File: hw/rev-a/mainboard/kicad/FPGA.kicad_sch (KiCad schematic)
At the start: 46 parts, among them J17 PMOD1, J18 PMOD2, J19 PROG, J4 BUS_EXPANSION, J9 FPGA_MCU, Q1 MMBT3904, SW3 CONFIG, U10 T8Q144C3

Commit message: hw: ren rev-c -> rev-a
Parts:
- removed C61: 10u, Capacitor_SMD:C_0603_1608Metric, symbol Device:C_Small
- added C66: 4u7 10V, Capacitor_SMD:C_0402_1005Metric, symbol Device:C_Small
- C62, C63, C64, C65: value 10u -> 4u7 10V; footprint Capacitor_SMD:C_0603_1608Metric -> Capacitor_SMD:C_0402_1005Metric; LCSC C96446 -> C23733
- D7: LCSC C72043 -> C2986059
- J17, J18: footprint PET:PMOD_Socket_2x06_P2.54mm_Horizontal -> EconoPET:PMOD_Socket_2x06_P2.54mm_Horizontal
- R26: renamed from R19; value 12k 1% -> 12k
- RN10, RN9: value 10k -> 10kx4
- SW3: footprint Button_Switch_THT:SW_DIP_SPSTx02_Slide_6.7x6.64mm_W7.62mm_P2.54mm_LowProfile -> EconoPET:SW_DIP_SPSTx02_Slide_6.7x6.64mm_W7.62mm_P2.54mm_LowProfile_or_SolderJumper
- U10: value T8Q144C3 -> T20Q144C3; footprint SnapEDA:QFP50P2200X2200X160-144N -> Package_QFP:LQFP-144_20x20mm_P0.5mm; symbol SnapEDA:T8Q144C3 -> EconoPET:T8Q144C3; LCSC C3278393 -> C3278392
- renumbered C38 to C39, C39 to C40, C40 to C41, C41 to C42, C42 to C43, C43 to C44, C44 to C45, C45 to C46, C46 to C47, C47 to C48, C48 to C49, C49 to C50, C50 to C51, C51 to C52, C52 to C53, C53 to C54, C54 to C55, C55 to C56, C56 to C57, C57 to C58, C58 to C59, C59 to C60, C60 to C61, J19 to J22, R17 to R24, R18 to R25, R20 to R27, R21 to R28, R22 to R29
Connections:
- net PD_GND is gone; now on net GND: C62.2, C63.2, J17.11 (Pin_11), J17.5 (Pin_5), J18.11 (Pin_11), J18.5 (Pin_5), SW3.1, SW3.2
- net +3V3: now also C65.1
- net +5V: now also C66.1; no longer C65.1
- net BE: now also U10.53 (GPIOB_TXP11); no longer U10.48 (GPIOB_TXN09)
- net CEC: now also J9.19 (Pin_19); no longer J9.20 (Pin_20)
- net DIAG: now also U10.39 (GPIOB_TXN00); no longer U10.38 (GPIOB_TXP00)
- net GND: now also C66.2
- net PHI2: now also U10.47 (GPIOB_TXP09); no longer U10.46 (GPIOB_TXN06)
- net PMOD1_1: now also U10.135 (GPIOL_72_EXTFB0_CDI14); no longer U10.118 (GPIOR_79_EXTFB1_CDI30)
- net PMOD1_2: now also U10.131 (GPIOL_75_PLLIN1); no longer U10.123 (GPIOR_77_PLLIN1)
- net PMOD1_3: now also U10.123 (GPIOR_77_PLLIN1); no longer U10.131 (GPIOL_75_PLLIN1)
- net PMOD1_4: now also U10.118 (GPIOR_79_EXTFB1_CDI30); no longer U10.135 (GPIOL_72_EXTFB0_CDI14)
- net PMOD1_5: now also U10.137 (GPIOL_70_CBSEL0); no longer U10.119 (GPIOR_78_EXTFB0_CDI31)
- net PMOD1_6: now also U10.134 (GPIOL_73_EXTFB1_CDI15); no longer U10.124 (GPIOR_76_PLLIN0)
- net PMOD1_7: now also U10.124 (GPIOR_76_PLLIN0); no longer U10.134 (GPIOL_73_EXTFB1_CDI15)
- net PMOD1_8: now also U10.119 (GPIOR_78_EXTFB0_CDI31); no longer U10.137 (GPIOL_70_CBSEL0)
- net PMOD2_1: now also U10.4 (GPIOL_54_CDI11); no longer U10.139 (GPIOL_68)
- net PMOD2_2: now also U10.144 (GPIOL_64); no longer U10.141 (GPIOL_65)
- net PMOD2_3: now also U10.141 (GPIOL_65); no longer U10.144 (GPIOL_64)
- net PMOD2_4: now also U10.139 (GPIOL_68); no longer U10.3 (GPIOL_53_CDI10)
- net PMOD2_5: now also U10.3 (GPIOL_53_CDI10); no longer U10.138 (GPIOL_69_CBSEL1)
- net PMOD2_6: now also U10.142 (GPIOL_66_CDI12); no longer U10.140 (GPIOL_67_CDI13)
- net PMOD2_7: now also U10.140 (GPIOL_67_CDI13); no longer U10.142 (GPIOL_66_CDI12)
- net PMOD2_8: now also U10.138 (GPIOL_69_CBSEL1); no longer U10.4 (GPIOL_54_CDI11)
- net RDY: now also U10.45 (GPIOB_TXP06); no longer U10.43 (GPIOB_TXN04)
- net SPI1_RX: now also J9.20 (Pin_20); no longer J9.19 (Pin_19)
- net SPI1_SCK: now also J9.15 (Pin_15); no longer J9.16 (Pin_16)
- net SPI1_~{READY}: now also J9.16 (Pin_16); no longer J9.15 (Pin_15)
- net VIA_CB2: now also U10.38 (GPIOB_TXP00); no longer U10.39 (GPIOB_TXN00)
- net ~{IRQ}: now also J4.5 (Pin_5), U10.46 (GPIOB_TXN06); no longer J4.8 (Pin_8), U10.47 (GPIOB_TXP09)
- net ~{ML}: now also U10.41 (GPIOB_TXN02); no longer U10.53 (GPIOB_TXP11)
- net ~{RES}: now also U10.43 (GPIOB_TXN04); no longer U10.42 (GPIOB_TXP04)
- net ~{SO}: now also J4.8 (Pin_8), U10.48 (GPIOB_TXN09); no longer J4.5 (Pin_5), U10.45 (GPIOB_TXP06)
- net ~{VP}: now also U10.42 (GPIOB_TXP04); no longer U10.41 (GPIOB_TXN02)
- no-connect marks 0 -> 1
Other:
- note added: "1% tolerance specified"

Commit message: hw: tidy schematics for publication
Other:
- note added: "TODO: Cleanup"
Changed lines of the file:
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@@
 		(date "2023-10-01")
 		(rev "A")
+		(comment 1 "Unspecified resistors are 1% and rated for 62.5mW or higher")
+		(comment 2 "Unspecified capacitors are rated for 25V or higher")
+		(comment 3 "Signals with B-prefix are level-shifted from 3V3 to 5V")
 	)
 	(junction
@@
 		)
 	)
+	(text "TODO: Cleanup"
+		(exclude_from_sim no)
+		(at 144.78 24.13 0)
+		(effects
+			(font
+				(size 2.54 2.54)
+				(thickness 0.508)
+				(bold yes)
+			)
+		)
+	)

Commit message: hw: tidy schematics for publication
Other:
- company: (none) -> https://is.gd/6hpvh6
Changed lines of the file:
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@@
 		(date "2023-10-01")
 		(rev "A")
-		(comment 1 "Unspecified resistors are 1% and rated for 62.5mW or higher")
-		(comment 2 "Unspecified capacitors are rated for 25V or higher")
+		(company "https://is.gd/6hpvh6")
+		(comment 1 "Unspecified resistors are 1% / 62.5mW")
+		(comment 2 "Unspecified capacitors are 25V")
 		(comment 3 "Signals with B-prefix are level-shifted from 3V3 to 5V")
+		(comment 4 "License: CC0 1.0 Universal (Public Domain Dedication)")
 	)
 	(junction

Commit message: hw: minor annotation on FPGA schematic
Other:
- note added: "During configuration, all GPIO pins excluding LVDS as GPIO are configured in weak pull-up mode. The LVDS as GPIO pins are tri-stated without a pull-up or pull-down resistor. Pull ~{CRESET} low to reset FPGA until MCU is ready. Note that MCU drives ~{CRESET} through 10k resistor so it can be overridden by programmer when connected. Pull CSI high to enable FPGA configuration Pull TEST_N high to dea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"
- note removed: "During configuration, all GPIO pins excluding LVDS as GPIO are configured in weak pull-up mode. The LVDS as GPIO pins are tri-stated without a pull-up or pull-down resistor."
- note removed: "Pull ~{CRESET} low to reset FPGA until MCU is ready. Note that MCU drives ~{CRESET} through 10k resistor so it can be overridden by programmer when connected. Pull CSI high to enable FPGA configuration Pull TEST_N high to deactivate test mode Pull CBUS[2:0] high for SPI x1 Leave CBSEL[1:0] floating (not using multi-image) MCU config: MCU drives SS_N low to select passive SPI MCU transitions CRESE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"
- moved on the sheet: C63, C64, C65, C66, D8, J17, J18, J4, R29

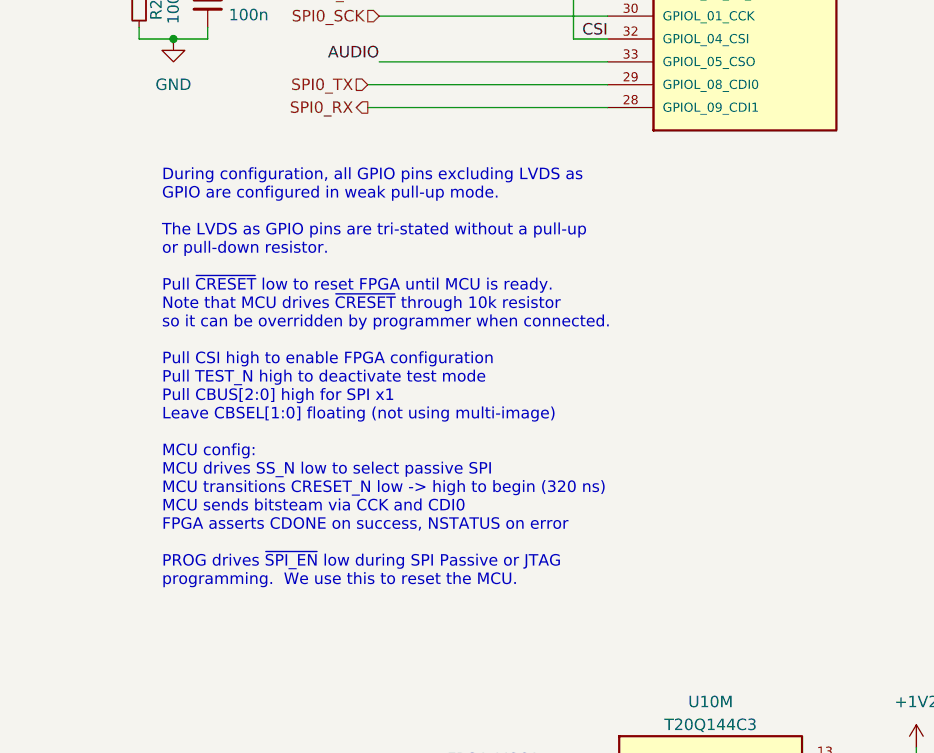
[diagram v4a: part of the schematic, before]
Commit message: hw: tidy schematic comment
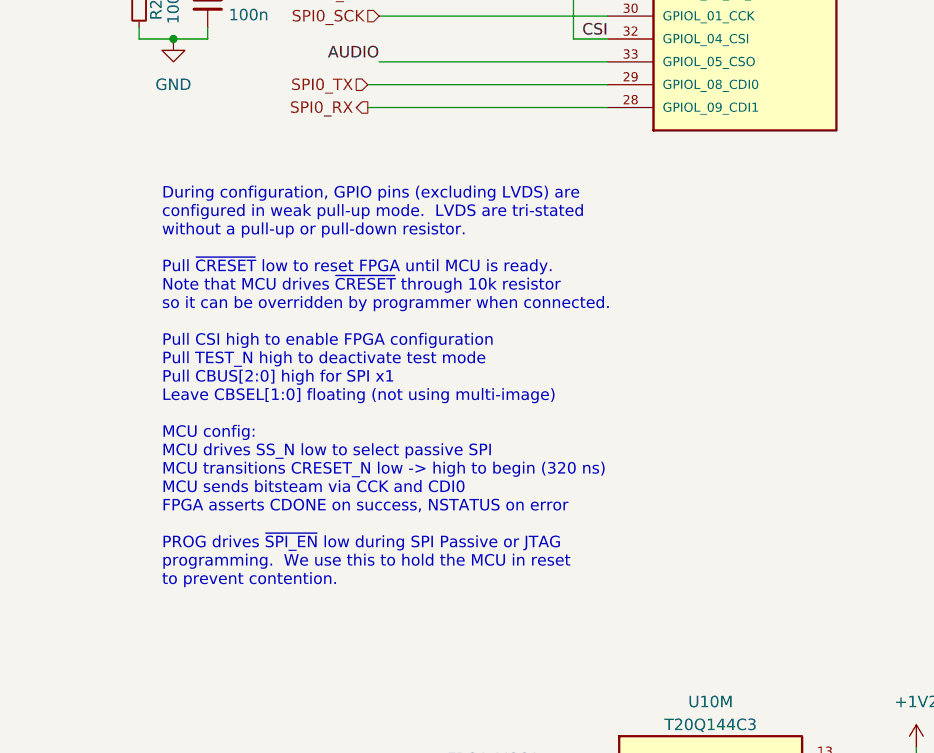
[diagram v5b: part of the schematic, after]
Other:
- note added: "During configuration, GPIO pins (excluding LVDS) are configured in weak pull-up mode. LVDS are tri-stated without a pull-up or pull-down resistor. Pull ~{CRESET} low to reset FPGA until MCU is ready. Note that MCU drives ~{CRESET} through 10k resistor so it can be overridden by programmer when connected. Pull CSI high to enable FPGA configuration Pull TEST_N high to deactivate test mode Pull CBUS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"
- note removed: "During configuration, all GPIO pins excluding LVDS as GPIO are configured in weak pull-up mode. The LVDS as GPIO pins are tri-stated without a pull-up or pull-down resistor. Pull ~{CRESET} low to reset FPGA until MCU is ready. Note that MCU drives ~{CRESET} through 10k resistor so it can be overridden by programmer when connected. Pull CSI high to enable FPGA configuration Pull TEST_N high to dea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"
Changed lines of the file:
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@@
 		)
 	)
-	(text "During configuration, all GPIO pins excluding LVDS as\nGPIO are configured in weak pull-up mode.\n\nThe LVDS as GPIO pins are tri-stated without a pull-up\nor pull-down resistor.\n\nPull ~{CRESET} low to reset FPGA until MCU is ready.\nNote that MCU drives ~{CRESET} through 10k resistor\nso it can be overridden by programmer when connected.\n\nPull CSI high to enable FPGA configuration\nPull TEST_N high to deactivate test mode\nPull CBUS[2:0] high for SPI x1\nLeave CBSEL[1:0] floating (not using multi-image)\n\nMCU config:\nMCU drives SS_N low to select passive SPI\nMCU transitions CRESET_N low -> high to begin (320 ns)\nMCU sends bitsteam via CCK and CDI0\nFPGA asserts CDONE on success, NSTATUS on error\n\nPROG drives ~{SPI_EN} low during SPI Passive or JTAG\nprogramming.  We use this to reset the MCU."
+	(text "During configuration, GPIO pins (excluding LVDS) are\nconfigured in weak pull-up mode.  LVDS are tri-stated\nwithout a pull-up or pull-down resistor.\n\nPull ~{CRESET} low to reset FPGA until MCU is ready.\nNote that MCU drives ~{CRESET} through 10k resistor\nso it can be overridden by programmer when connected.\n\nPull CSI high to enable FPGA configuration\nPull TEST_N high to deactivate test mode\nPull CBUS[2:0] high for SPI x1\nLeave CBSEL[1:0] floating (not using multi-image)\n\nMCU config:\nMCU drives SS_N low to select passive SPI\nMCU transitions CRESET_N low -> high to begin (320 ns)\nMCU sends bitsteam via CCK and CDI0\nFPGA asserts CDONE on success, NSTATUS on error\n\nPROG drives ~{SPI_EN} low during SPI Passive or JTAG\nprogramming.  We use this to hold the MCU in reset\nto prevent contention."
 		(exclude_from_sim no)
 		(at 17.78 125.73 0)
